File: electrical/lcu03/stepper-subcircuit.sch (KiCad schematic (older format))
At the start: 12 parts, among them P14 stepper_conn, U8 a4985

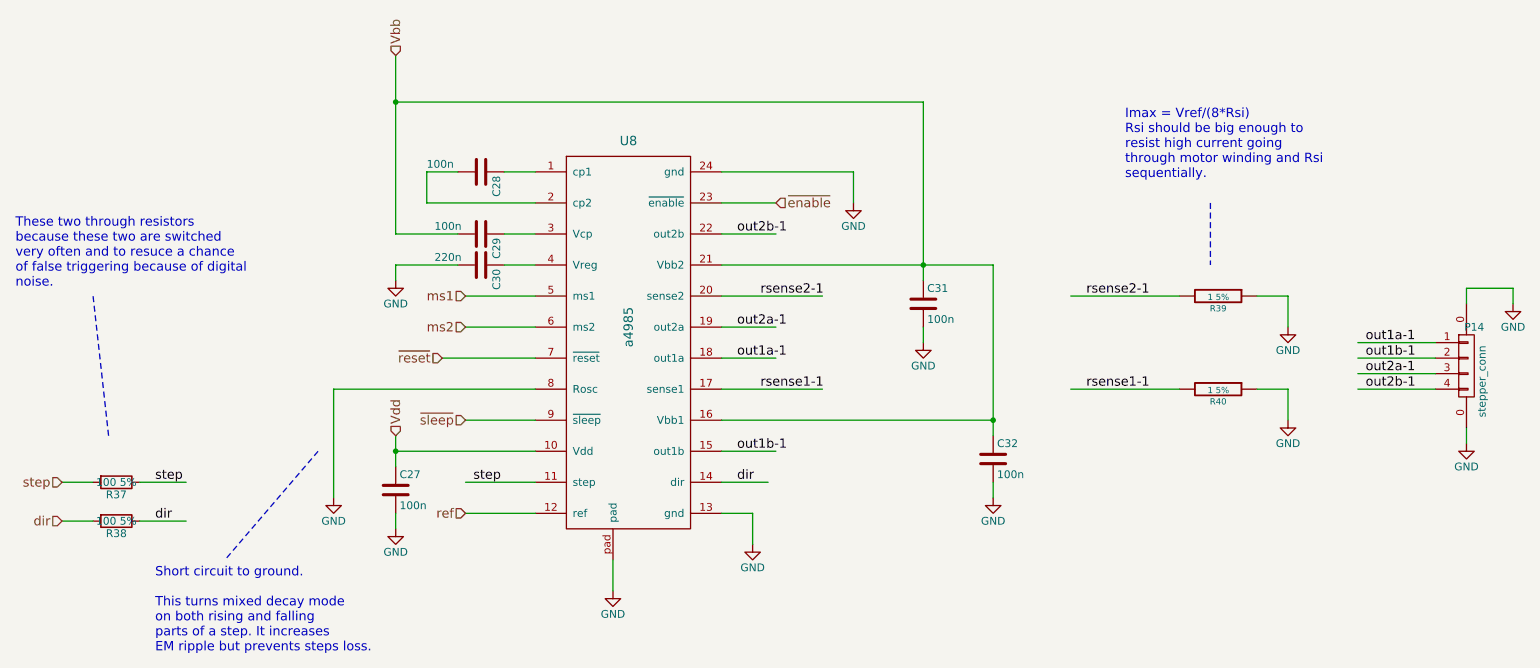
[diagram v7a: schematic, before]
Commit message: Started placing components.
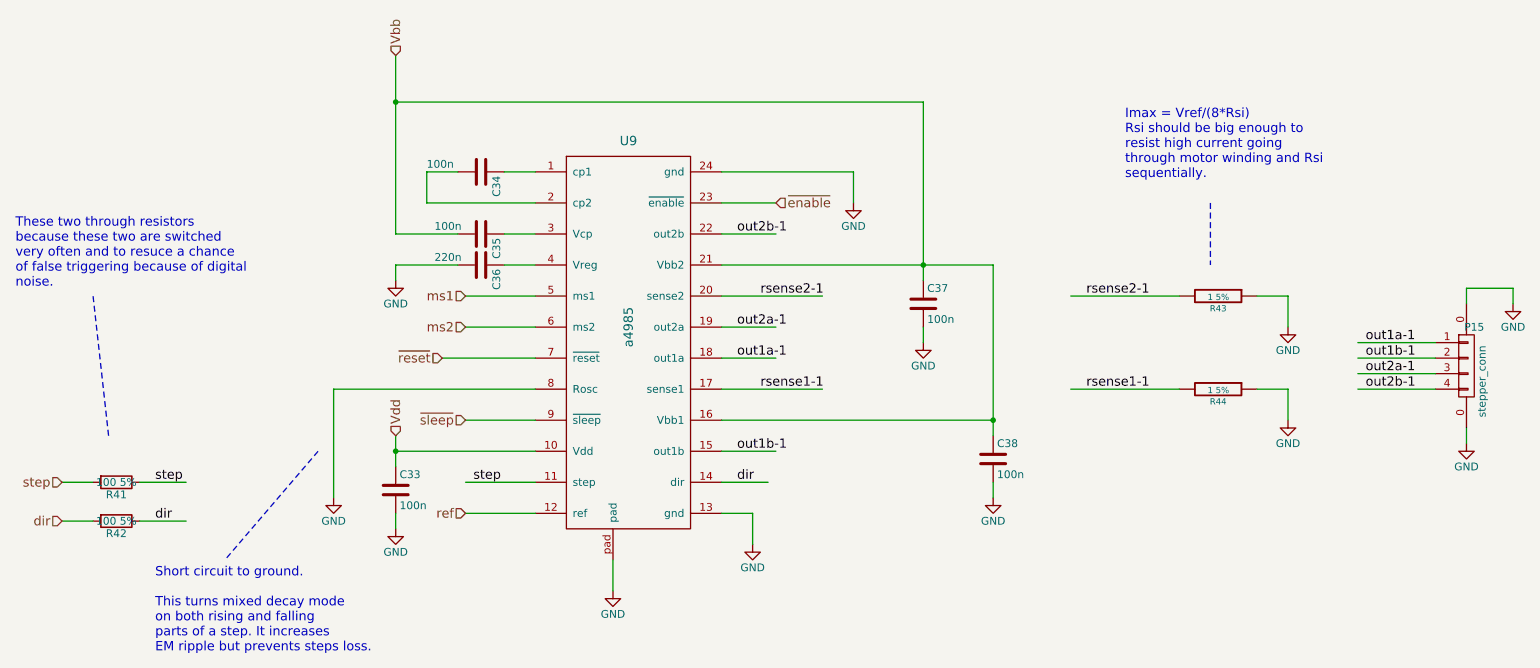
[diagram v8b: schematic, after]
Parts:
- P14: footprint Connectors_JST_PH:Connectors_JST_B4B-PH-SM4-TB -> my-lib:JST_B4B-PH-SM4-TB
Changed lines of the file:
@@
 AR Path="/5667C1E7/5667C673" Ref="U8"  Part="1"
 AR Path="/56687F5B/5667C673" Ref="U9"  Part="1"
-F 0 "U8" H 4650 4550 60  0000 C CNN
+F 0 "U9" H 4650 4550 60  0000 C CNN
 F 1 "a4985" V 4650 3350 60  0000 C CNN
 F 2 "my-lib:a4985" H 4650 3350 60  0001 C CNN
@@
 AR Path="/5667C1E7/5667C682" Ref="C28"  Part="1"
 AR Path="/56687F5B/5667C682" Ref="C34"  Part="1"
-F 0 "C28" H 3725 2450 50  0000 L CNN
+F 0 "C34" H 3725 2450 50  0000 L CNN
 F 1 "100n" V 3650 2000 50  0000 L CNN
 F 2 "Capacitors_SMD:C_0805" H 3738 2200 50  0001 C CNN
@@
 AR Path="/5667C1E7/5667C68D" Ref="C29"  Part="1"
 AR Path="/56687F5B/5667C68D" Ref="C35"  Part="1"
-F 0 "C29" H 3725 2850 50  0000 L CNN
+F 0 "C35" H 3725 2850 50  0000 L CNN
 F 1 "100n" V 3650 2450 50  0000 L CNN
 F 2 "Capacitors_SMD:C_0805" H 3738 2600 50  0001 C CNN
@@
 AR Path="/5667C1E7/5667C697" Ref="C30"  Part="1"
 AR Path="/56687F5B/5667C697" Ref="C36"  Part="1"
-F 0 "C30" H 3725 3050 50  0000 L CNN
+F 0 "C36" H 3725 3050 50  0000 L CNN
 F 1 "220n" V 3650 2650 50  0000 L CNN
 F 2 "Capacitors_SMD:C_0805" H 3738 2800 50  0001 C CNN
@@
 AR Path="/5667C1E7/5667C6A1" Ref="#PWR095"  Part="1"
 AR Path="/56687F5B/5667C6A1" Ref="#PWR0107"  Part="1"
-F 0 "#PWR095" H 3150 2800 50  0001 C CNN
+F 0 "#PWR0107" H 3150 2800 50  0001 C CNN
 F 1 "GND" H 3150 2900 50  0000 C CNN
 F 2 "" H 3150 3050 50  0000 C CNN
@@
 AR Path="/5667C1E7/5667C6AF" Ref="C27"  Part="1"
 AR Path="/56687F5B/5667C6AF" Ref="C33"  Part="1"
-F 0 "C27" H 3175 4500 50  0000 L CNN
+F 0 "C33" H 3175 4500 50  0000 L CNN
 F 1 "100n" H 3175 4300 50  0000 L CNN
 F 2 "Capacitors_SMD:C_0805" H 3188 4250 50  0001 C CNN
@@
 AR Path="/5667C1E7/5667C6B8" Ref="#PWR096"  Part="1"
 AR Path="/56687F5B/5667C6B8" Ref="#PWR0108"  Part="1"
-F 0 "#PWR096" H 3150 4400 50  0001 C CNN
+F 0 "#PWR0108" H 3150 4400 50  0001 C CNN
 F 1 "GND" H 3150 4500 50  0000 C CNN
 F 2 "" H 3150 4650 50  0000 C CNN
@@
 AR Path="/5667C1E7/5667C6C4" Ref="#PWR097"  Part="1"
 AR Path="/56687F5B/5667C6C4" Ref="#PWR0109"  Part="1"
-F 0 "#PWR097" H 5450 4500 50  0001 C CNN
+F 0 "#PWR0109" H 5450 4500 50  0001 C CNN
 F 1 "GND" H 5450 4600 50  0000 C CNN
 F 2 "" H 5450 4750 50  0000 C CNN
@@
 AR Path="/5667C1E7/5667C6CB" Ref="#PWR098"  Part="1"
 AR Path="/56687F5B/5667C6CB" Ref="#PWR0110"  Part="1"
-F 0 "#PWR098" H 4550 4800 50  0001 C CNN
+F 0 "#PWR0110" H 4550 4800 50  0001 C CNN
 F 1 "GND" H 4550 4900 50  0000 C CNN
 F 2 "" H 4550 5050 50  0000 C CNN
@@
 AR Path="/5667C1E7/5667C6DE" Ref="#PWR099"  Part="1"
 AR Path="/56687F5B/5667C6DE" Ref="#PWR0111"  Part="1"
-F 0 "#PWR099" H 2750 4200 50  0001 C CNN
+F 0 "#PWR0111" H 2750 4200 50  0001 C CNN
 F 1 "GND" H 2750 4300 50  0000 C CNN
 F 2 "" H 2750 4450 50  0000 C CNN
@@
 AR Path="/5667C1E7/5667C6E6" Ref="#PWR0100"  Part="1"
 AR Path="/56687F5B/5667C6E6" Ref="#PWR0112"  Part="1"
-F 0 "#PWR0100" H 6550 3200 50  0001 C CNN
+F 0 "#PWR0112" H 6550 3200 50  0001 C CNN
 F 1 "GND" H 6550 3300 50  0000 C CNN
 F 2 "" H 6550 3450 50  0000 C CNN
@@
 AR Path="/5667C1E7/5667C6ED" Ref="#PWR0101"  Part="1"
 AR Path="/56687F5B/5667C6ED" Ref="#PWR0113"  Part="1"
-F 0 "#PWR0101" H 7000 4200 50  0001 C CNN
+F 0 "#PWR0113" H 7000 4200 50  0001 C CNN
 F 1 "GND" H 7000 4300 50  0000 C CNN
 F 2 "" H 7000 4450 50  0000 C CNN
@@
 AR Path="/5667C1E7/5667C6F4" Ref="R39"  Part="1"
 AR Path="/56687F5B/5667C6F4" Ref="R43"  Part="1"
-F 0 "R39" V 8530 3150 40  0000 C CNN
+F 0 "R43" V 8530 3150 40  0000 C CNN
 F 1 "1 5%" V 8457 3151 40  0000 C CNN
 F 2 "Resistors_SMD:R_0805" V 8380 3150 30  0001 C CNN
@@
 AR Path="/5667C1E7/5667C701" Ref="C31"  Part="1"
 AR Path="/56687F5B/5667C701" Ref="C37"  Part="1"
-F 0 "C31" H 6575 3300 50  0000 L CNN
+F 0 "C37" H 6575 3300 50  0000 L CNN
 F 1 "100n" H 6575 3100 50  0000 L CNN
 F 2 "Capacitors_SMD:C_0805" H 6588 3050 50  0001 C CNN
@@
 AR Path="/5667C1E7/5667C708" Ref="C32"  Part="1"
 AR Path="/56687F5B/5667C708" Ref="C38"  Part="1"
-F 0 "C32" H 7025 4300 50  0000 L CNN
+F 0 "C38" H 7025 4300 50  0000 L CNN
 F 1 "100n" H 7025 4100 50  0000 L CNN
 F 2 "Capacitors_SMD:C_0805" H 7038 4050 50  0001 C CNN
@@
 AR Path="/5667C1E7/5667C713" Ref="#PWR0102"  Part="1"
 AR Path="/56687F5B/5667C713" Ref="#PWR0114"  Part="1"
-F 0 "#PWR0102" H 8900 3100 50  0001 C CNN
+F 0 "#PWR0114" H 8900 3100 50  0001 C CNN
 F 1 "GND" H 8900 3200 50  0000 C CNN
 F 2 "" H 8900 3350 50  0000 C CNN
@@
 AR Path="/5667C1E7/5667C719" Ref="R40"  Part="1"
 AR Path="/56687F5B/5667C719" Ref="R44"  Part="1"
-F 0 "R40" V 8530 3750 40  0000 C CNN
+F 0 "R44" V 8530 3750 40  0000 C CNN
 F 1 "1 5%" V 8457 3751 40  0000 C CNN
 F 2 "Resistors_SMD:R_0805" V 8380 3750 30  0001 C CNN
@@
 AR Path="/5667C1E7/5667C724" Ref="#PWR0103"  Part="1"
 AR Path="/56687F5B/5667C724" Ref="#PWR0115"  Part="1"
-F 0 "#PWR0103" H 8900 3700 50  0001 C CNN
+F 0 "#PWR0115" H 8900 3700 50  0001 C CNN
 F 1 "GND" H 8900 3800 50  0000 C CNN
 F 2 "" H 8900 3950 50  0000 C CNN
@@
 AR Path="/5667C1E7/5667C72E" Ref="#PWR0104"  Part="1"
 AR Path="/56687F5B/5667C72E" Ref="#PWR0116"  Part="1"
-F 0 "#PWR0104" H 6100 2300 50  0001 C CNN
+F 0 "#PWR0116" H 6100 2300 50  0001 C CNN
 F 1 "GND" H 6100 2400 50  0000 C CNN
 F 2 "" H 6100 2550 50  0000 C CNN
@@
 AR Path="/5667C1E7/566C867B" Ref="R37"  Part="1"
 AR Path="/56687F5B/566C867B" Ref="R41"  Part="1"
-F 0 "R37" V 1430 4350 50  0000 C CNN
+F 0 "R41" V 1430 4350 50  0000 C CNN
 F 1 "100 5%" V 1350 4350 50  0000 C CNN
 F 2 "Resistors_SMD:R_0805" V 1280 4350 50  0001 C CNN
@@
 AR Path="/5667C1E7/566C8917" Ref="R38"  Part="1"
 AR Path="/56687F5B/566C8917" Ref="R42"  Part="1"
-F 0 "R38" V 1430 4600 50  0000 C CNN
+F 0 "R42" V 1430 4600 50  0000 C CNN
 F 1 "100 5%" V 1350 4600 50  0000 C CNN
 F 2 "Resistors_SMD:R_0805" V 1280 4600 50  0001 C CNN
@@
 AR Path="/5667C1E7/5668FCA0" Ref="P14"  Part="1"
 AR Path="/56687F5B/5668FCA0" Ref="P15"  Part="1"
-F 0 "P14" H 10100 3850 50  0000 C CNN
+F 0 "P15" H 10100 3850 50  0000 C CNN
 F 1 "stepper_conn" V 10150 3500 50  0000 C CNN
-F 2 "Connectors_JST_PH:Connectors_JST_B4B-PH-SM4-TB" H 10050 3600 50  0001 C CNN
+F 2 "my-lib:JST_B4B-PH-SM4-TB" H 10050 3600 50  0001 C CNN
 F 3 "" H 10050 3600 50  0000 C CNN
 	1    10050 3600
@@
 AR Path="/5667C1E7/5668FCAB" Ref="#PWR0105"  Part="1"
 AR Path="/56687F5B/5668FCAB" Ref="#PWR0117"  Part="1"
-F 0 "#PWR0105" H 10050 3850 50  0001 C CNN
+F 0 "#PWR0117" H 10050 3850 50  0001 C CNN
 F 1 "GND" H 10050 3950 50  0000 C CNN
 F 2 "" H 10050 4100 60  0000 C CNN
@@
 AR Path="/5667C1E7/5668FCB1" Ref="#PWR0106"  Part="1"
 AR Path="/56687F5B/5668FCB1" Ref="#PWR0118"  Part="1"
-F 0 "#PWR0106" H 10350 2950 50  0001 C CNN
+F 0 "#PWR0118" H 10350 2950 50  0001 C CNN
 F 1 "GND" H 10350 3050 50  0000 C CNN
 F 2 "" H 10350 3200 60  0000 C CNN
